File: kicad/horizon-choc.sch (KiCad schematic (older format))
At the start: 121 parts, among them SW1 SW_Push, SW10 SW_Push, SW11 SW_Push, SW12 SW_Push, SW13 SW_Push, SW14 SW_Push, SW15 SW_Push, SW16 SW_Push, SW17 SW_Push, SW18 SW_Push, SW19 SW_Push, SW2 SW_Push, SW20 SW_Push, SW21 SW_Push, SW22 SW_Push, SW23 SW_Push, SW24 SW_Push, SW25 SW_Push, SW26 SW_Push, SW27 SW_Push, SW28 SW_Push, SW29 SW_Push, SW3 SW_Push, SW30 SW_Push, SW31 SW_Push, SW32 SW_Push, SW33 SW_Push, SW34 SW_Push, SW35 SW_Push, SW36 SW_Push, SW37 SW_Push, SW38 SW_Push, SW39 SW_Push, SW4 SW_Push, SW40 SW_Push, SW41 SW_Push, SW42 SW_Push, SW43 SW_Push, SW44 SW_Push, SW45 SW_Push, SW46 SW_Push, SW47 SW_Push, SW48 SW_Push, SW49 SW_Push, SW5 SW_Push, SW50 SW_Push, SW51 SW_Push, SW52 SW_Push, SW6 SW_Push, SW7 SW_Push, SW8 SW_Push, SW9 SW_Push, U1 PRO-MICRO

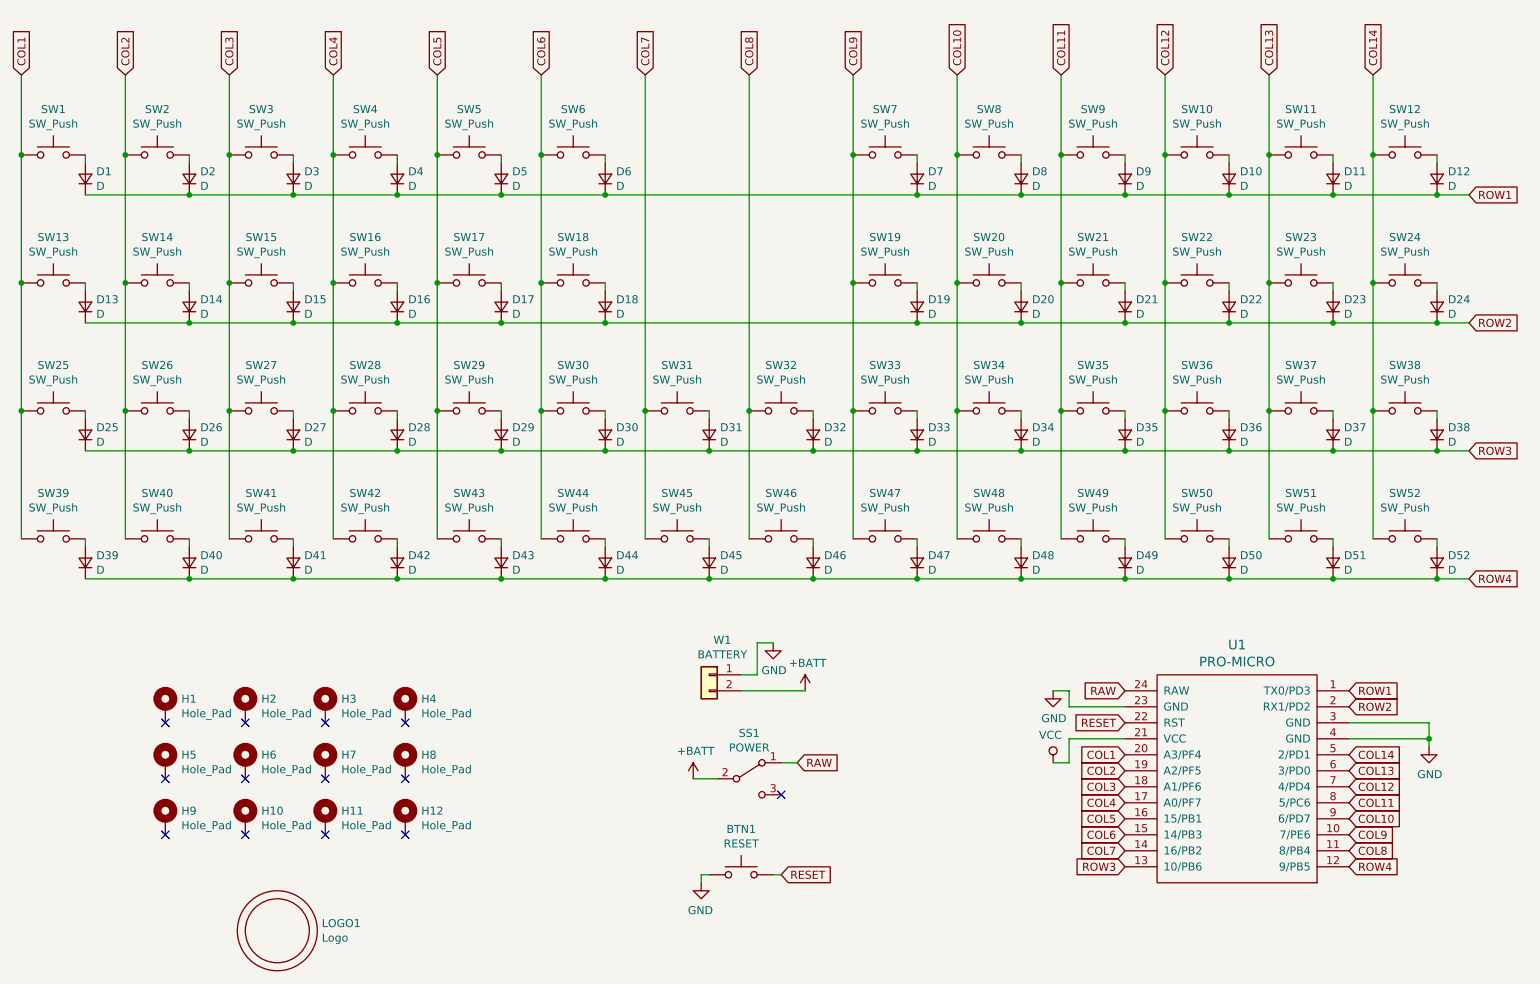
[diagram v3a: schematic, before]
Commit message: Use 50-key layout
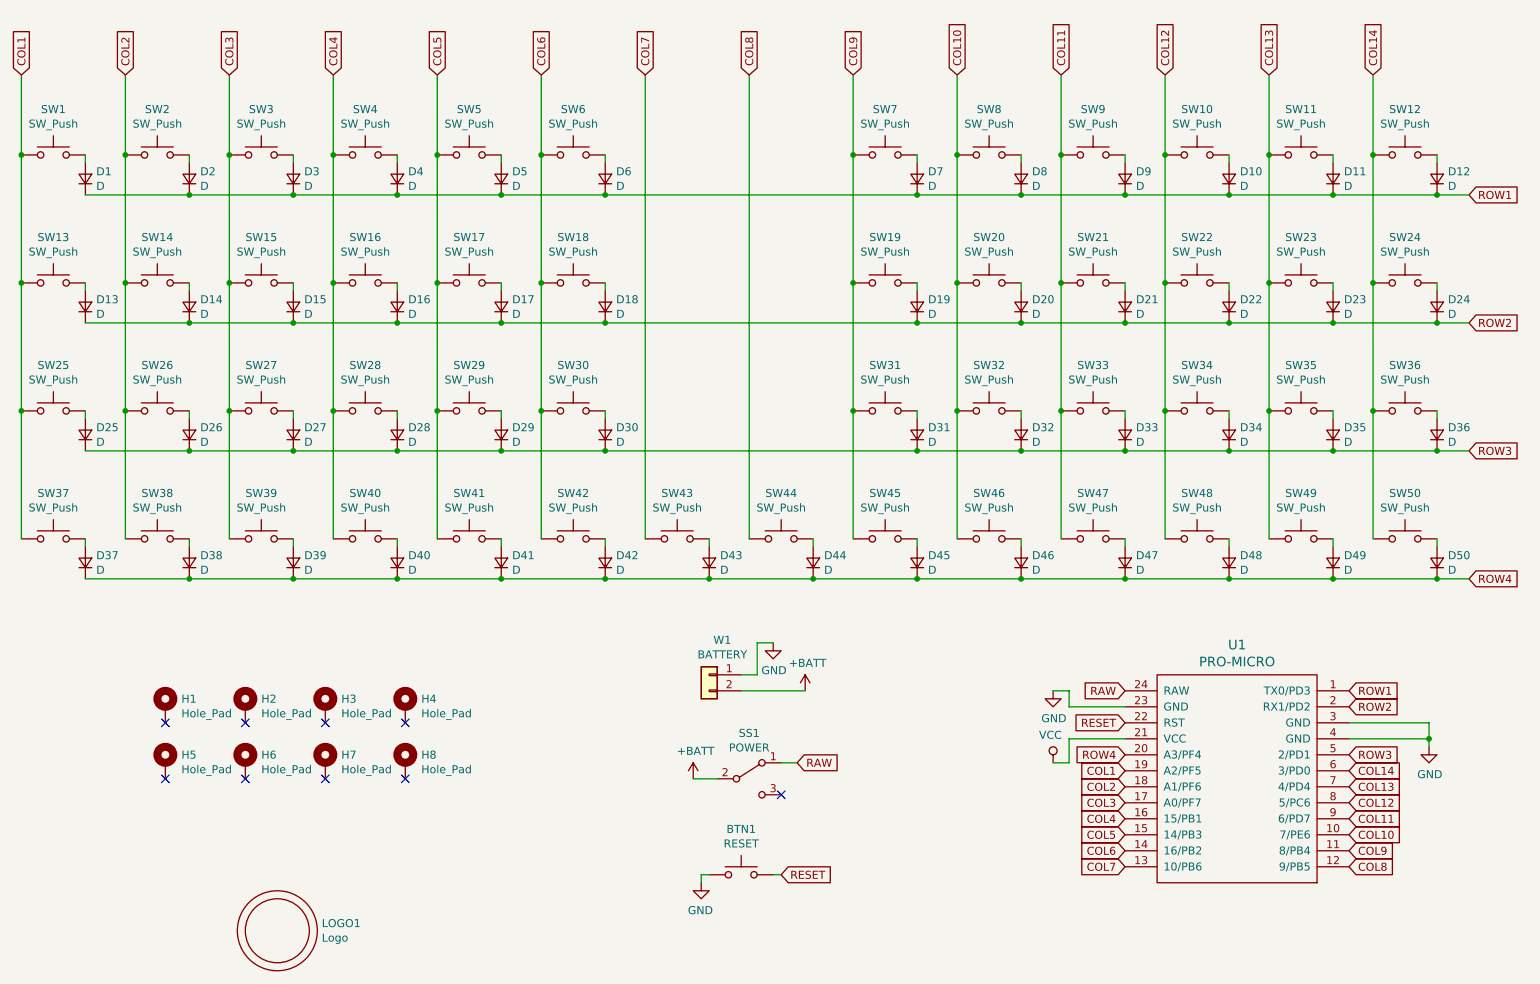
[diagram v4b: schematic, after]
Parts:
- removed D31, D32: D, horizon-footprints:D_SOD-123, symbol horizon-components:D
- removed H10, H11, H12, H9: Hole_Pad, horizon-footprints:Mount_M2, symbol horizon-components:Hole_Pad
- removed SW31, SW32: SW_Push, horizon-footprints:SW_Choc, symbol horizon-components:SW_Push
- renumbered D33 to D31, D34 to D32, D35 to D33, D36 to D34, D37 to D35, D38 to D36, D39 to D37, D40 to D38, D41 to D39, D42 to D40, D43 to D41, D44 to D42, D45 to D43, D46 to D44, D47 to D45, D48 to D46, D49 to D47, D50 to D48, D51 to D49, D52 to D50, SW33 to SW31, SW34 to SW32, SW35 to SW33, SW36 to SW34, SW37 to SW35, SW38 to SW36, SW39 to SW37, SW40 to SW38, SW41 to SW39, SW42 to SW40, SW43 to SW41, SW44 to SW42, SW45 to SW43, SW46 to SW44, SW47 to SW45, SW48 to SW46, SW49 to SW47, SW50 to SW48, SW51 to SW49, SW52 to SW50
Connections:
- net COL1: now also U1.19 (A2/PF5); no longer U1.20 (A3/PF4)
- net COL10: now also U1.10 (7/PE6); no longer U1.9 (6/PD7)
- net COL11: now also U1.9 (6/PD7); no longer U1.8 (5/PC6)
- net COL12: now also U1.8 (5/PC6); no longer U1.7 (4/PD4)
- net COL13: now also U1.7 (4/PD4); no longer U1.6 (3/PD0)
- net COL14: now also U1.6 (3/PD0); no longer U1.5 (2/PD1)
- net COL2: now also U1.18 (A1/PF6); no longer U1.19 (A2/PF5)
- net COL3: now also U1.17 (A0/PF7); no longer U1.18 (A1/PF6)
- net COL4: now also U1.16 (15/PB1); no longer U1.17 (A0/PF7)
- net COL5: now also U1.15 (14/PB3); no longer U1.16 (15/PB1)
- net COL6: now also U1.14 (16/PB2); no longer U1.15 (14/PB3)
- net COL7: now also U1.13 (10/PB6); no longer U1.14 (16/PB2)
- net COL8: now also U1.12 (9/PB5); no longer U1.11 (8/PB4)
- net COL9: now also U1.11 (8/PB4); no longer U1.10 (7/PE6)
- net ROW3: now also U1.5 (2/PD1); no longer U1.13 (10/PB6)
- net ROW4: now also U1.20 (A3/PF4); no longer U1.12 (9/PB5)
- no-connect marks 13 -> 9

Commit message: Layout MX PCB
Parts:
- added D31, D32: D, horizon-footprints:D_SOD-123, symbol horizon-components:D
- added SW31, SW32: SW_Push, horizon-footprints:SW_Choc, symbol horizon-components:SW_Push
- LOGO1: footprint horizon-footprints:Logo_Horizon -> horizon-footprints:Logo_Horizon_Small
- TB1: renamed from W1; footprint horizon-footprints:Battery_Wire_Pads -> horizon-footprints:KF350-2P
- renumbered D31 to D33, D32 to D34, D33 to D35, D34 to D36, D35 to D37, D36 to D38, D37 to D39, D38 to D40, D39 to D41, D40 to D42, D41 to D43, D42 to D44, D43 to D45, D44 to D46, D45 to D47, D46 to D48, D47 to D49, D48 to D50, D49 to D51, D50 to D52, SW31 to SW33, SW32 to SW34, SW33 to SW35, SW34 to SW36, SW35 to SW37, SW36 to SW38, SW37 to SW39, SW38 to SW40, SW39 to SW41, SW40 to SW42, SW41 to SW43, SW42 to SW44, SW43 to SW45, SW44 to SW46, SW45 to SW47, SW46 to SW48, SW47 to SW49, SW48 to SW50, SW49 to SW51, SW50 to SW52
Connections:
- net COL7: now also SW31.1
- net COL8: now also SW32.1
- net RAW: now also SS1.3 (C); no longer SS1.1 (A)
- net ROW3: now also D31.1 (K), D32.1 (K)
- new net: D31.2 (A), SW31.2
- new net: D32.2 (A), SW32.2

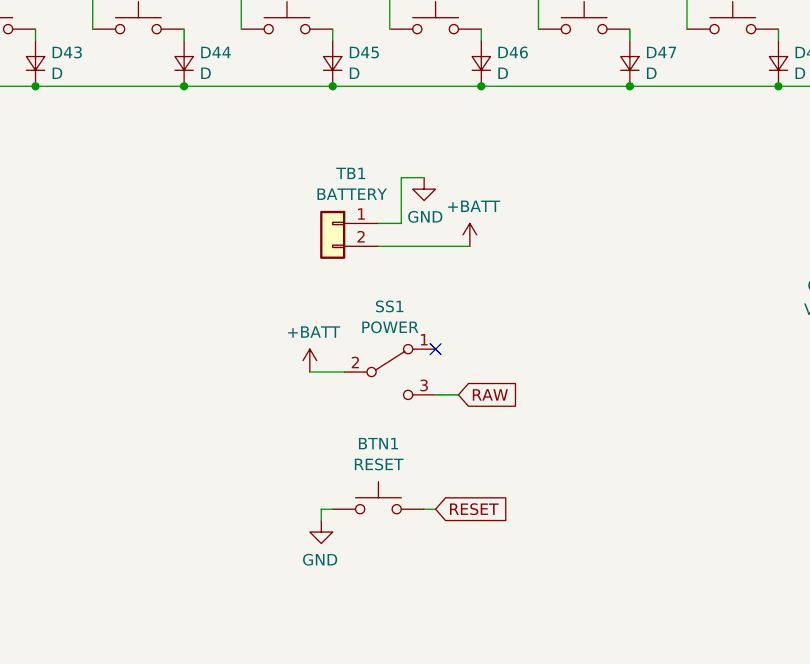
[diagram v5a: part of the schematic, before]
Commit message: Update plate outlines. Remove battery from Choc design for now
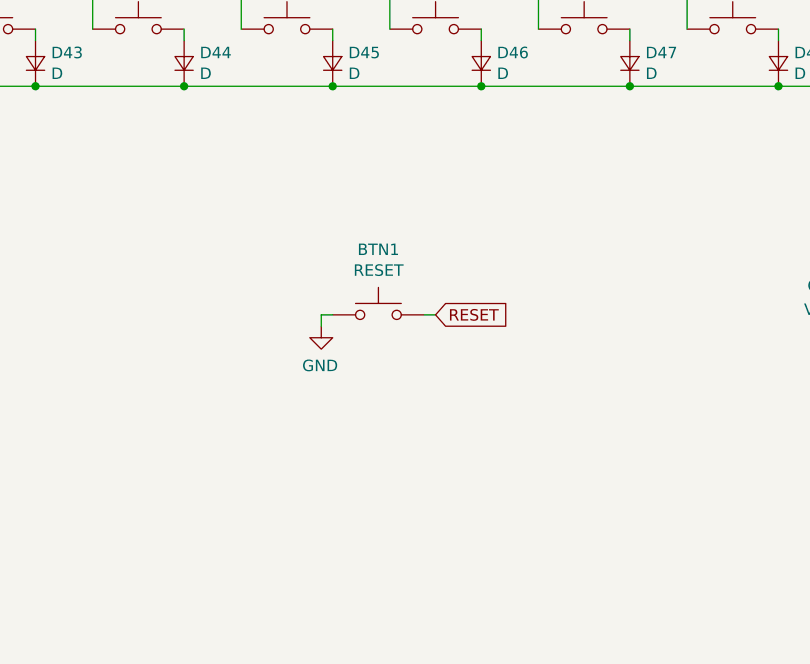
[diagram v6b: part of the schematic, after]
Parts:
- removed SS1: POWER, horizon-footprints:SS12D00, symbol horizon-components:SW_SPDT
- removed TB1: BATTERY, horizon-footprints:KF350-2P, symbol horizon-components:Conn_01x02
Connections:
- no-connect marks 9 -> 8
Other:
- moved on the sheet: BTN1
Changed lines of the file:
@@
 L horizon-components:SW_Push BTN1
 U 1 1 60FA8D3C
-P 5300 6050
-F 0 "BTN1" H 5300 6335 50  0000 C CNN
-F 1 "RESET" H 5300 6244 50  0000 C CNN
-F 2 "horizon-footprints:SW_Push_6mm" H 5300 6250 50  0001 C CNN
-F 3 "~" H 5300 6250 50  0001 C CNN
-	1    5300 6050
+P 5300 5200
+F 0 "BTN1" H 5300 5485 50  0000 C CNN
+F 1 "RESET" H 5300 5394 50  0000 C CNN
+F 2 "horizon-footprints:SW_Push_6mm" H 5300 5400 50  0001 C CNN
+F 3 "~" H 5300 5400 50  0001 C CNN
+	1    5300 5200
 	-1   0    0    -1
 $EndComp
-Text GLabel 5550 6050 2    50   Input ~ 0
+Text GLabel 5550 5200 2    50   Input ~ 0
 RESET
 Wire Wire Line
-	5550 6050 5500 6050
+	5550 5200 5500 5200
 $Comp
 L power:GND #PWR07
 U 1 1 60FB8E05
-P 5050 6100
-F 0 "#PWR07" H 5050 5850 50  0001 C CNN
-F 1 "GND" H 5055 5927 50  0000 C CNN
-F 2 "" H 5050 6100 50  0001 C CNN
-F 3 "" H 5050 6100 50  0001 C CNN
-	1    5050 6100
+P 5050 5250
+F 0 "#PWR07" H 5050 5000 50  0001 C CNN
+F 1 "GND" H 5055 5077 50  0000 C CNN
+F 2 "" H 5050 5250 50  0001 C CNN
+F 3 "" H 5050 5250 50  0001 C CNN
+	1    5050 5250
 	-1   0    0    -1
 $EndComp
 Wire Wire Line
-	5100 6050 5050 6050
+	5100 5200 5050 5200
 Wire Wire Line
-	5050 6050 5050 6100
-Text GLabel 5650 5550 2    50   Input ~ 0
-RAW
-Wire Wire Line
-	5150 5450 5000 5450
-$Comp
-L power:+BATT #PWR06
-U 1 1 618AF3B6
-P 5000 5450
-F 0 "#PWR06" H 5000 5300 50  0001 C CNN
-F 1 "+BATT" H 5015 5623 50  0000 C CNN
-F 2 "" H 5000 5450 50  0001 C CNN
-F 3 "" H 5000 5450 50  0001 C CNN
-	1    5000 5450
-	1    0    0    -1
-$EndComp
-Wire Wire Line
-	5650 5550 5550 5550
-Wire Wire Line
-	5300 4900 5700 4900
-$Comp
-L power:+BATT #PWR02
-U 1 1 6182DFC2
-P 5700 4900
-F 0 "#PWR02" H 5700 4750 50  0001 C CNN
-F 1 "+BATT" H 5715 5073 50  0000 C CNN
-F 2 "" H 5700 4900 50  0001 C CNN
-F 3 "" H 5700 4900 50  0001 C CNN
-	1    5700 4900
-	1    0    0    -1
-$EndComp
-$Comp
-L power:GND #PWR01
-U 1 1 617240FF
-P 5500 4600
-F 0 "#PWR01" H 5500 4350 50  0001 C CNN
-F 1 "GND" H 5505 4427 50  0000 C CNN
-F 2 "" H 5500 4600 50  0001 C CNN
-F 3 "" H 5500 4600 50  0001 C CNN
-	1    5500 4600
-	1    0    0    -1
-$EndComp
-$Comp
-L horizon-components:Conn_01x02 TB1
-U 1 1 617240F0
-P 5100 4800
-F 0 "TB1" H 5018 5017 50  0000 C CNN
-F 1 "BATTERY" H 5018 4926 50  0000 C CNN
-F 2 "horizon-footprints:KF350-2P" H 5100 4800 50  0001 C CNN
-F 3 "~" H 5100 4800 50  0001 C CNN
-	1    5100 4800
-	-1   0    0    -1
-$EndComp
-Wire Wire Line
-	5300 4800 5400 4800
-Wire Wire Line
-	5400 4800 5400 4600
-Wire Wire Line
-	5400 4600 5500 4600
+	5050 5200 5050 5250
 $Comp
 L horizon-components:D D31
@@
 Text GLabel 7700 5400 0    50   Input ~ 0
 COL1
-$Comp
-L horizon-components:SW_SPDT SS1
-U 1 1 617240F8
-P 5350 5450
-F 0 "SS1" H 5350 5735 50  0000 C CNN
-F 1 "POWER" H 5350 5644 50  0000 C CNN
-F 2 "horizon-footprints:SS12D00" H 5350 5450 50  0001 C CNN
-F 3 "~" H 5350 5450 50  0001 C CNN
-	1    5350 5450
-	1    0    0    -1
-$EndComp
-NoConn ~ 5550 5350
 $EndSCHEMATC
